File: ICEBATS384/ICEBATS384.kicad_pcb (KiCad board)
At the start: 4 copper layers, 30 x 15 mm, 36 parts, among them J1 513389873, J2 5017450401, U1 ICE40LP384-SG32, U2 W25X40CLUXIG TR, U4 NCP114AMX120TCG, Y1 ASCO

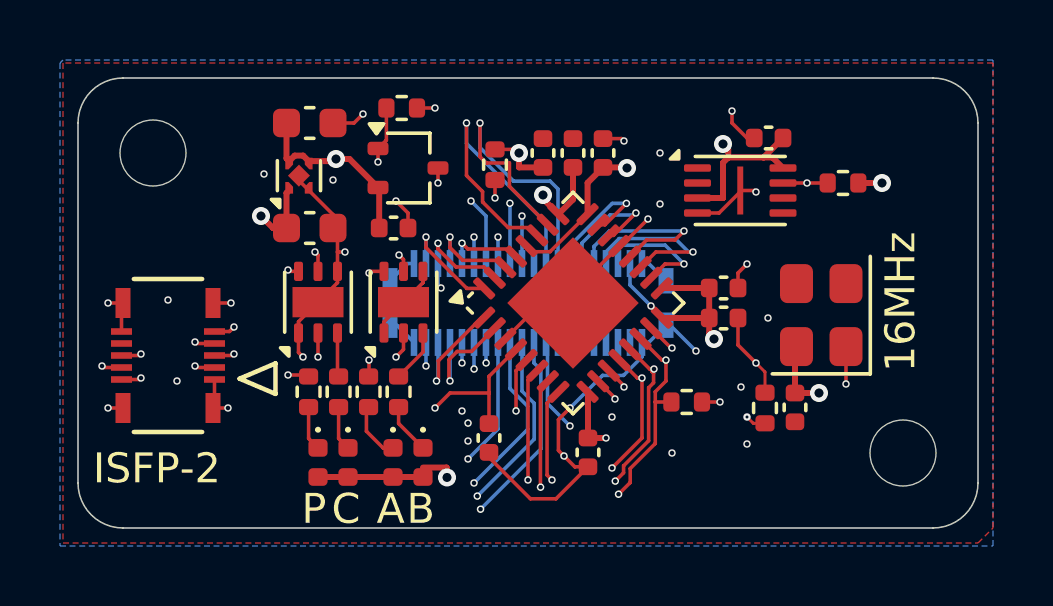
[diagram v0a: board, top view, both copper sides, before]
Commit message: Fixes missing schematic connections.
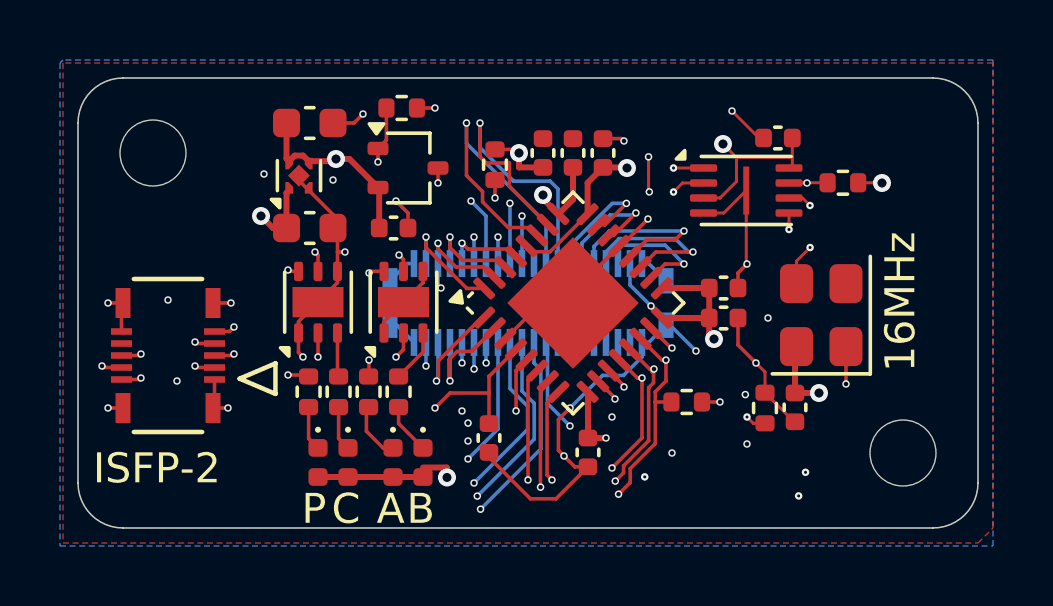
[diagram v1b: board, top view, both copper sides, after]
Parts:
- moved C8 0.31 mm to (48.3, 34.5)
- moved U2 0.20 mm to (47.3, 36.2)
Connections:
- J2 pad 35: F_IO6 -> CLOCK
- Q1 pad 7: (no net) -> GND
- Q2 pad 7: (no net) -> GND
- U1 pad 6: F_IO6 -> CLOCK
- U2 pad 1: F_|SS -> F_IO14
- U2 pad 2: F_SI -> F_IO13
- U2 pad 5: F_SO -> F_IO12
- U2 pad 6: F_SCK -> F_IO15
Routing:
- net CLOCK: track 0.00 -> 29.9 mm, vias 0 -> 5
- net F_IO12: track 32.0 -> 45.5 mm, vias 4 -> 5
- net F_IO6: track 10.7 -> 0.00 mm, vias 3 -> 0
- net F_IO15: track 27.7 -> 37.8 mm, vias 4 -> 5
- net F_IO14: track 38.1 -> 46.0 mm, vias 4 -> 5
- net F_IO13: track 32.2 -> 39.6 mm, vias 4 -> 5
- net GND: track 47.9 -> 51.3 mm, vias 18 -> 17
- net +3V3: track 43.0 -> 44.2 mm, vias 21 -> 23
